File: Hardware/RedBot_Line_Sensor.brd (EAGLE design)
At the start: 7.6 x 24.1 mm, 11 parts, among them U1 QRE1113SMD-W

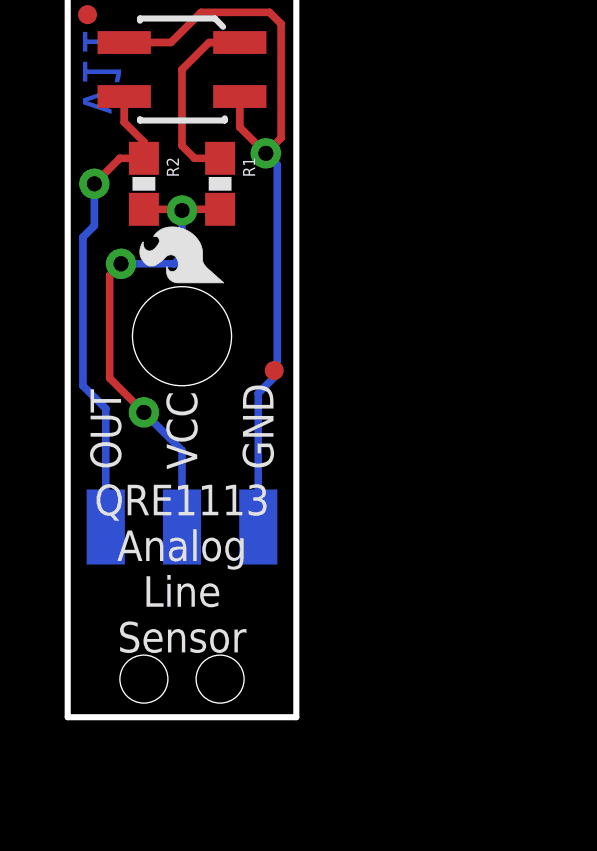
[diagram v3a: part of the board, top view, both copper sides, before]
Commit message: Silk fixes and trace reroutes
Fixed top silk so pin labels are closer to edge of board and nothing
gets cut off. Removed flame from top. Cleaned up "out" and "vcc" traces
to be more efficient.
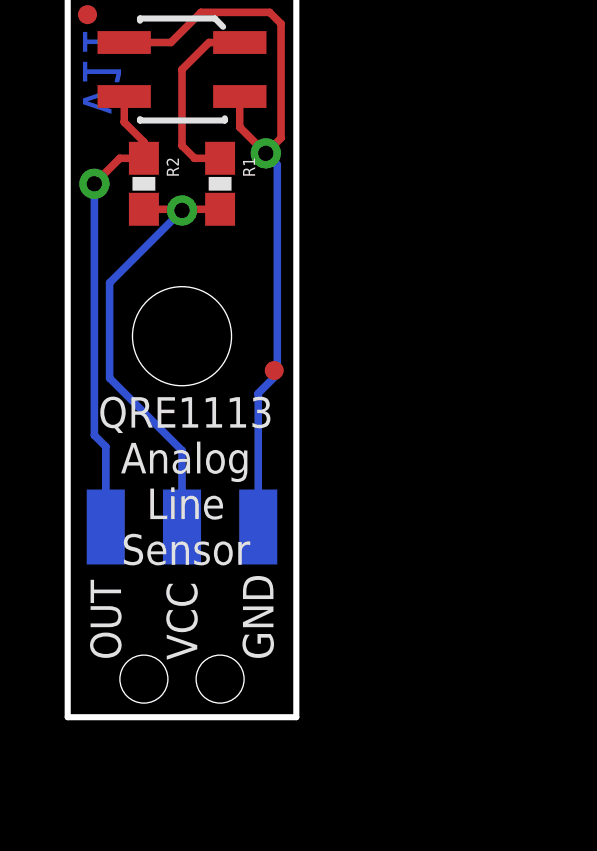
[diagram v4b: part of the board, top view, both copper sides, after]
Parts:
- removed LOGO1: LOGO-SFESK, SparkFun-Aesthetics:SFE-LOGO-FLAME
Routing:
- net 5V: track 16.2 -> 15.1 mm, vias 3 -> 1

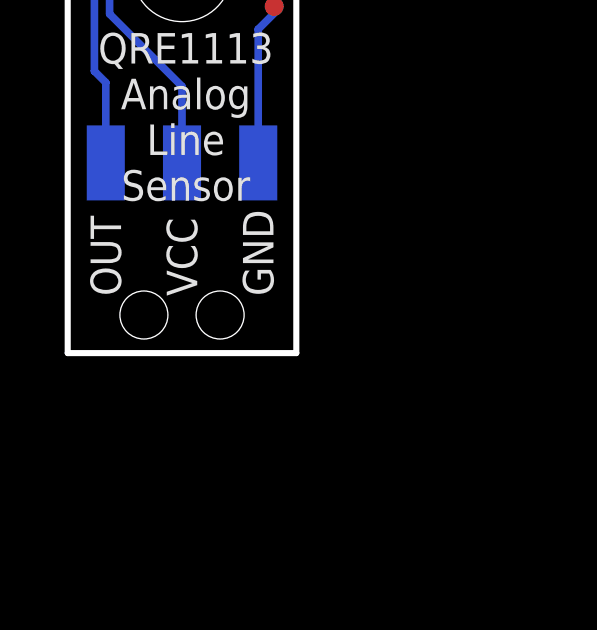
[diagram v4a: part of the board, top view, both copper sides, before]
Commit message: Updating 3 pin connector package
Updating 3 pin connector package to use new footprint that drops drill
hits for the connector's bosses down from 0.062' to 0.0535'. This will
help keep the part straight during reflow.
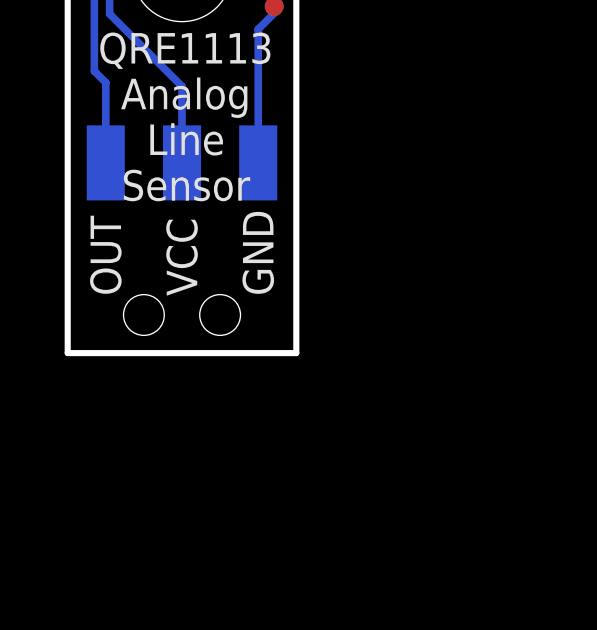
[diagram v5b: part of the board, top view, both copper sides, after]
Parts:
- JP1: device SparkFun-Connectors:1X03_SMD_RA_MALE_POST -> SparkFun-Connectors:1X03_SMD_RA_MALE_POST_SMALLER
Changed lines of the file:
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@@
 <layer number="54" name="bGND_GNDA" color="1" fill="9" visible="no" active="no"/>
 <layer number="56" name="wert" color="7" fill="1" visible="no" active="no"/>
+<layer number="57" name="tCAD" color="7" fill="1" visible="no" active="no"/>
 <layer number="91" name="Nets" color="2" fill="1" visible="no" active="no"/>
 <layer number="92" name="Busses" color="1" fill="1" visible="no" active="no"/>
@@
 <layer number="97" name="Info" color="7" fill="1" visible="no" active="no"/>
 <layer number="98" name="Guide" color="6" fill="1" visible="no" active="no"/>
+<layer number="99" name="SpiceOrder" color="7" fill="1" visible="no" active="no"/>
 <layer number="100" name="Muster" color="7" fill="1" visible="no" active="no"/>
 <layer number="101" name="Patch_Top" color="12" fill="4" visible="no" active="no"/>
@@
 <layer number="108" name="tplace-old" color="10" fill="1" visible="no" active="yes"/>
 <layer number="109" name="ref-old" color="11" fill="1" visible="no" active="yes"/>
+<layer number="110" name="fp0" color="7" fill="1" visible="no" active="yes"/>
+<layer number="111" name="LPC17xx" color="7" fill="1" visible="no" active="yes"/>
+<layer number="112" name="tSilk" color="7" fill="1" visible="no" active="yes"/>
+<layer number="113" name="IDFDebug" color="4" fill="1" visible="no" active="yes"/>
 <layer number="116" name="Patch_BOT" color="9" fill="4" visible="no" active="no"/>
 <layer number="121" name="_tsilk" color="7" fill="1" visible="no" active="no"/>
 <layer number="122" name="_bsilk" color="7" fill="1" visible="no" active="no"/>
+<layer number="123" name="tTestmark" color="7" fill="1" visible="no" active="yes"/>
+<layer number="124" name="bTestmark" color="7" fill="1" visible="no" active="yes"/>
 <layer number="125" name="_tNames" color="7" fill="1" visible="no" active="no"/>
+<layer number="126" name="_bNames" color="7" fill="1" visible="no" active="yes"/>
+<layer number="127" name="_tValues" color="7" fill="1" visible="no" active="yes"/>
+<layer number="128" name="_bValues" color="7" fill="1" visible="no" active="yes"/>
+<layer number="131" name="tAdjust" color="7" fill="1" visible="no" active="yes"/>
+<layer number="132" name="bAdjust" color="7" fill="1" visible="no" active="yes"/>
 <layer number="144" name="Drill_legend" color="7" fill="1" visible="no" active="no"/>
+<layer number="150" name="Notes" color="7" fill="1" visible="no" active="yes"/>
 <layer number="151" name="HeatSink" color="7" fill="1" visible="no" active="no"/>
+<layer number="152" name="_bDocu" color="7" fill="1" visible="no" active="yes"/>
+<layer number="153" name="FabDoc1" color="7" fill="1" visible="no" active="yes"/>
+<layer number="154" name="FabDoc2" color="7" fill="1" visible="no" active="yes"/>
+<layer number="155" name="FabDoc3" color="7" fill="1" visible="no" active="yes"/>
 <layer number="199" name="Contour" color="7" fill="1" visible="no" active="no"/>
 <layer number="200" name="200bmp" color="1" fill="10" visible="no" active="no"/>
@@
 <layer number="223" name="223bmp" color="24" fill="1" visible="no" active="no"/>
 <layer number="224" name="224bmp" color="25" fill="1" visible="no" active="no"/>
+<layer number="248" name="Housing" color="7" fill="1" visible="no" active="yes"/>
+<layer number="249" name="Edge" color="7" fill="1" visible="no" active="yes"/>
 <layer number="250" name="Descript" color="3" fill="1" visible="no" active="no"/>
 <layer number="251" name="SMDround" color="12" fill="11" visible="no" active="no"/>
@@
 <attribute name="PROD_ID" value="RES-00824" x="-22.86" y="-20.32" size="1.778" layer="27" rot="R270" display="off"/>
 </element>
-<element name="JP1" library="SparkFun-Connectors" package="1X03_SMD_RA_MALE_POST" value="" x="3.81" y="1.27" rot="MR0"/>
+<element name="JP1" library="SparkFun-Connectors" package="1X03_SMD_RA_MALE_POST_SMALLER" value="" x="3.81" y="1.27" rot="MR0"/>
 <element name="STANDOFF1" library="SparkFun-Electromechanical" package="STAND-OFF" value="STAND-OFF" x="3.81" y="12.7"/>
 <element name="LOGO3" library="SparkFun-Aesthetics" package="SFE-LOGO-FLAME" value="LOGO-SFESK" x="4.826" y="17.272" rot="MR0"/>

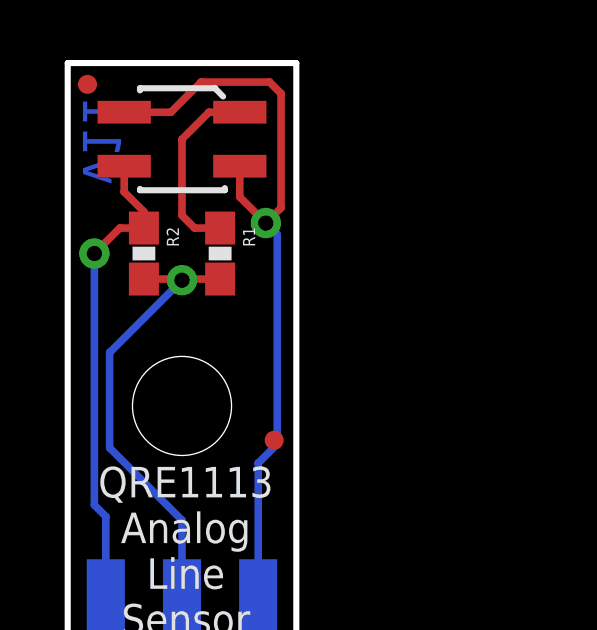
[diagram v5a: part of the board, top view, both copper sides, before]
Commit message: removed micro fid. added regular
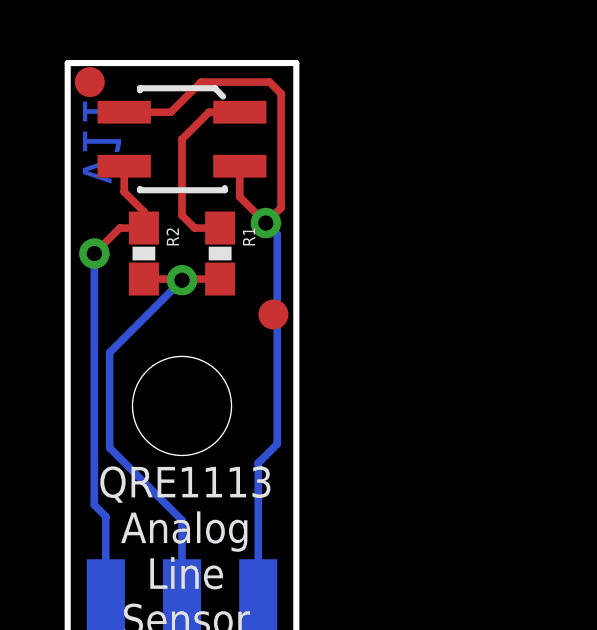
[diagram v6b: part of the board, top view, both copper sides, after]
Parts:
- FID1, FID2: value FIDUCIALUFIDUCIAL -> FIDUCIAL1X2; device SparkFun-Aesthetics:MICRO-FIDUCIAL -> SparkFun-Aesthetics:FIDUCIAL-1X2
- moved FID1 13.4 mm to (0.74, 23.5)
- moved FID2 9.86 mm to (6.86, 15.7)
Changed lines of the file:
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@@
 <?xml version="1.0" encoding="utf-8"?>
 <!DOCTYPE eagle SYSTEM "eagle.dtd">
-<eagle version="6.5.0">
+<eagle version="6.6.0">
 <drawing>
 <settings>
@@
 <setting verticaltext="up"/>
 </settings>
-<grid distance="0.05" unitdist="inch" unit="inch" style="lines" multiple="1" display="yes" altdistance="0.005" altunitdist="inch" altunit="inch"/>
+<grid distance="0.01" unitdist="inch" unit="inch" style="lines" multiple="1" display="yes" altdistance="0.001" altunitdist="inch" altunit="inch"/>
 <layers>
 <layer number="1" name="Top" color="4" fill="1" visible="yes" active="yes"/>
-<layer number="2" name="Route2" color="1" fill="3" visible="no" active="yes"/>
-<layer number="15" name="Route15" color="4" fill="6" visible="no" active="yes"/>
+<layer number="2" name="Route2" color="1" fill="3" visible="yes" active="yes"/>
+<layer number="15" name="Route15" color="4" fill="6" visible="yes" active="yes"/>
 <layer number="16" name="Bottom" color="1" fill="1" visible="yes" active="yes"/>
 <layer number="17" name="Pads" color="2" fill="1" visible="yes" active="yes"/>
 <layer number="18" name="Vias" color="2" fill="1" visible="yes" active="yes"/>
 <layer number="19" name="Unrouted" color="6" fill="1" visible="yes" active="yes"/>
-<layer number="20" name="Dimension" color="15" fill="1" visible="yes" active="yes"/>
-<layer number="21" name="tPlace" color="16" fill="1" visible="yes" active="yes"/>
-<layer number="22" name="bPlace" color="14" fill="1" visible="yes" active="yes"/>
+<layer number="20" name="Dimension" color="6" fill="1" visible="yes" active="yes"/>
+<layer number="21" name="tPlace" color="6" fill="1" visible="yes" active="yes"/>
+<layer number="22" name="bPlace" color="6" fill="1" visible="yes" active="yes"/>
 <layer number="23" name="tOrigins" color="15" fill="1" visible="yes" active="yes"/>
 <layer number="24" name="bOrigins" color="15" fill="1" visible="yes" active="yes"/>
-<layer number="25" name="tNames" color="7" fill="1" visible="no" active="yes"/>
-<layer number="26" name="bNames" color="7" fill="1" visible="no" active="yes"/>
-<layer number="27" name="tValues" color="7" fill="1" visible="no" active="yes"/>
-<layer number="28" name="bValues" color="7" fill="1" visible="no" active="yes"/>
-<layer number="29" name="tStop" color="7" fill="3" visible="no" active="yes"/>
-<layer number="30" name="bStop" color="7" fill="6" visible="no" active="yes"/>
-<layer number="31" name="tCream" color="7" fill="4" visible="no" active="yes"/>
-<layer number="32" name="bCream" color="7" fill="5" visible="no" active="yes"/>
-<layer number="39" name="tKeepout" color="4" fill="11" visible="no" active="yes"/>
-<layer number="40" name="bKeepout" color="1" fill="11" visible="no" active="yes"/>
-<layer number="41" name="tRestrict" color="4" fill="10" visible="no" active="yes"/>
-<layer number="42" name="bRestrict" color="1" fill="10" visible="no" active="yes"/>
-<layer number="44" name="Drills" color="7" fill="1" visible="no" active="yes"/>
+<layer number="25" name="tNames" color="7" fill="1" visible="yes" active="yes"/>
+<layer number="26" name="bNames" color="7" fill="1" visible="yes" active="yes"/>
+<layer number="27" name="tValues" color="7" fill="1" visible="yes" active="yes"/>
+<layer number="28" name="bValues" color="7" fill="1" visible="yes" active="yes"/>
+<layer number="29" name="tStop" color="7" fill="3" visible="yes" active="yes"/>
+<layer number="30" name="bStop" color="7" fill="6" visible="yes" active="yes"/>
+<layer number="31" name="tCream" color="7" fill="4" visible="yes" active="yes"/>
+<layer number="32" name="bCream" color="7" fill="5" visible="yes" active="yes"/>
+<layer number="39" name="tKeepout" color="4" fill="11" visible="yes" active="yes"/>
+<layer number="40" name="bKeepout" color="1" fill="11" visible="yes" active="yes"/>
+<layer number="41" name="tRestrict" color="4" fill="10" visible="yes" active="yes"/>
+<layer number="42" name="bRestrict" color="1" fill="10" visible="yes" active="yes"/>
+<layer number="44" name="Drills" color="7" fill="1" visible="yes" active="yes"/>
 <layer number="45" name="Holes" color="7" fill="1" visible="yes" active="yes"/>
-<layer number="46" name="Milling" color="3" fill="1" visible="no" active="yes"/>
+<layer number="46" name="Milling" color="3" fill="1" visible="yes" active="yes"/>
 <layer number="51" name="tDocu" color="6" fill="1" visible="yes" active="yes"/>
-<layer number="52" name="bDocu" color="7" fill="1" visible="no" active="yes"/>
+<layer number="52" name="bDocu" color="7" fill="1" visible="yes" active="yes"/>
 <layer number="3" name="Route3" color="4" fill="3" visible="no" active="no"/>
 <layer number="4" name="Route4" color="1" fill="4" visible="no" active="no"/>
@@
 <layer number="106" name="bPlate" color="7" fill="1" visible="no" active="no"/>
 <layer number="107" name="Crop" color="7" fill="1" visible="no" active="no"/>
-<layer number="108" name="tplace-old" color="10" fill="1" visible="no" active="yes"/>
-<layer number="109" name="ref-old" color="11" fill="1" visible="no" active="yes"/>
-<layer number="110" name="fp0" color="7" fill="1" visible="no" active="yes"/>
-<layer number="111" name="LPC17xx" color="7" fill="1" visible="no" active="yes"/>
-<layer number="112" name="tSilk" color="7" fill="1" visible="no" active="yes"/>
-<layer number="113" name="IDFDebug" color="4" fill="1" visible="no" active="yes"/>
+<layer number="108" name="tplace-old" color="10" fill="1" visible="yes" active="yes"/>
+<layer number="109" name="ref-old" color="11" fill="1" visible="yes" active="yes"/>
+<layer number="110" name="fp0" color="7" fill="1" visible="yes" active="yes"/>
+<layer number="111" name="LPC17xx" color="7" fill="1" visible="yes" active="yes"/>
+<layer number="112" name="tSilk" color="7" fill="1" visible="yes" active="yes"/>
+<layer number="113" name="IDFDebug" color="4" fill="1" visible="yes" active="yes"/>
 <layer number="116" name="Patch_BOT" color="9" fill="4" visible="no" active="no"/>
 <layer number="121" name="_tsilk" color="7" fill="1" visible="no" active="no"/>
 <layer number="122" name="_bsilk" color="7" fill="1" visible="no" active="no"/>
-<layer number="123" name="tTestmark" color="7" fill="1" visible="no" active="yes"/>
-<layer number="124" name="bTestmark" color="7" fill="1" visible="no" active="yes"/>
+<layer number="123" name="tTestmark" color="7" fill="1" visible="yes" active="yes"/>
+<layer number="124" name="bTestmark" color="7" fill="1" visible="yes" active="yes"/>
 <layer number="125" name="_tNames" color="7" fill="1" visible="no" active="no"/>
-<layer number="126" name="_bNames" color="7" fill="1" visible="no" active="yes"/>
-<layer number="127" name="_tValues" color="7" fill="1" visible="no" active="yes"/>
-<layer number="128" name="_bValues" color="7" fill="1" visible="no" active="yes"/>
-<layer number="131" name="tAdjust" color="7" fill="1" visible="no" active="yes"/>
-<layer number="132" name="bAdjust" color="7" fill="1" visible="no" active="yes"/>
+<layer number="126" name="_bNames" color="7" fill="1" visible="yes" active="yes"/>
+<layer number="127" name="_tValues" color="7" fill="1" visible="yes" active="yes"/>
+<layer number="128" name="_bValues" color="7" fill="1" visible="yes" active="yes"/>
+<layer number="131" name="tAdjust" color="7" fill="1" visible="yes" active="yes"/>
+<layer number="132" name="bAdjust" color="7" fill="1" visible="yes" active="yes"/>
 <layer number="144" name="Drill_legend" color="7" fill="1" visible="no" active="no"/>
-<layer number="150" name="Notes" color="7" fill="1" visible="no" active="yes"/>
+<layer number="150" name="Notes" color="7" fill="1" visible="yes" active="yes"/>
 <layer number="151" name="HeatSink" color="7" fill="1" visible="no" active="no"/>
-<layer number="152" name="_bDocu" color="7" fill="1" visible="no" active="yes"/>
-<layer number="153" name="FabDoc1" color="7" fill="1" visible="no" active="yes"/>
-<layer number="154" name="FabDoc2" color="7" fill="1" visible="no" active="yes"/>
-<layer number="155" name="FabDoc3" color="7" fill="1" visible="no" active="yes"/>
+<layer number="152" name="_bDocu" color="7" fill="1" visible="yes" active="yes"/>
+<layer number="153" name="FabDoc1" color="7" fill="1" visible="yes" active="yes"/>
+<layer number="154" name="FabDoc2" color="7" fill="1" visible="yes" active="yes"/>
+<layer number="155" name="FabDoc3" color="7" fill="1" visible="yes" active="yes"/>
 <layer number="199" name="Contour" color="7" fill="1" visible="no" active="no"/>
 <layer number="200" name="200bmp" color="1" fill="10" visible="no" active="no"/>
@@
 <layer number="223" name="223bmp" color="24" fill="1" visible="no" active="no"/>
 <layer number="224" name="224bmp" color="25" fill="1" visible="no" active="no"/>
-<layer number="248" name="Housing" color="7" fill="1" visible="no" active="yes"/>
-<layer number="249" name="Edge" color="7" fill="1" visible="no" active="yes"/>
+<layer number="248" name="Housing" color="7" fill="1" visible="yes" active="yes"/>
+<layer number="249" name="Edge" color="7" fill="1" visible="yes" active="yes"/>
 <layer number="250" name="Descript" color="3" fill="1" visible="no" active="no"/>
 <layer number="251" name="SMDround" color="12" fill="11" visible="no" active="no"/>
@@
 <element name="STANDOFF1" library="SparkFun-Electromechanical" package="STAND-OFF" value="STAND-OFF" x="3.81" y="12.7"/>
 <element name="LOGO3" library="SparkFun-Aesthetics" package="SFE-LOGO-FLAME" value="LOGO-SFESK" x="4.826" y="17.272" rot="MR0"/>
-<element name="FID1" library="SparkFun-Aesthetics" package="MICRO-FIDUCIAL" value="FIDUCIALUFIDUCIAL" x="6.8834" y="11.557"/>
-<element name="FID2" library="SparkFun-Aesthetics" package="MICRO-FIDUCIAL" value="FIDUCIALUFIDUCIAL" x="0.6604" y="23.4188"/>
+<element name="FID1" library="SparkFun-Aesthetics" package="FIDUCIAL-1X2" value="FIDUCIAL1X2" x="0.7366" y="23.495"/>
+<element name="FID2" library="SparkFun-Aesthetics" package="FIDUCIAL-1X2" value="FIDUCIAL1X2" x="6.858" y="15.748"/>
 </elements>
 <signals>
